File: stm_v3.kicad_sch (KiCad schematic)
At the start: 35 parts, among them Q1 s8050, Q2 s8050, SW1 RST, SW2 BOOT0, U1 STM32L431RCTx, U2 SN65HVD231, Y1 16 MHz

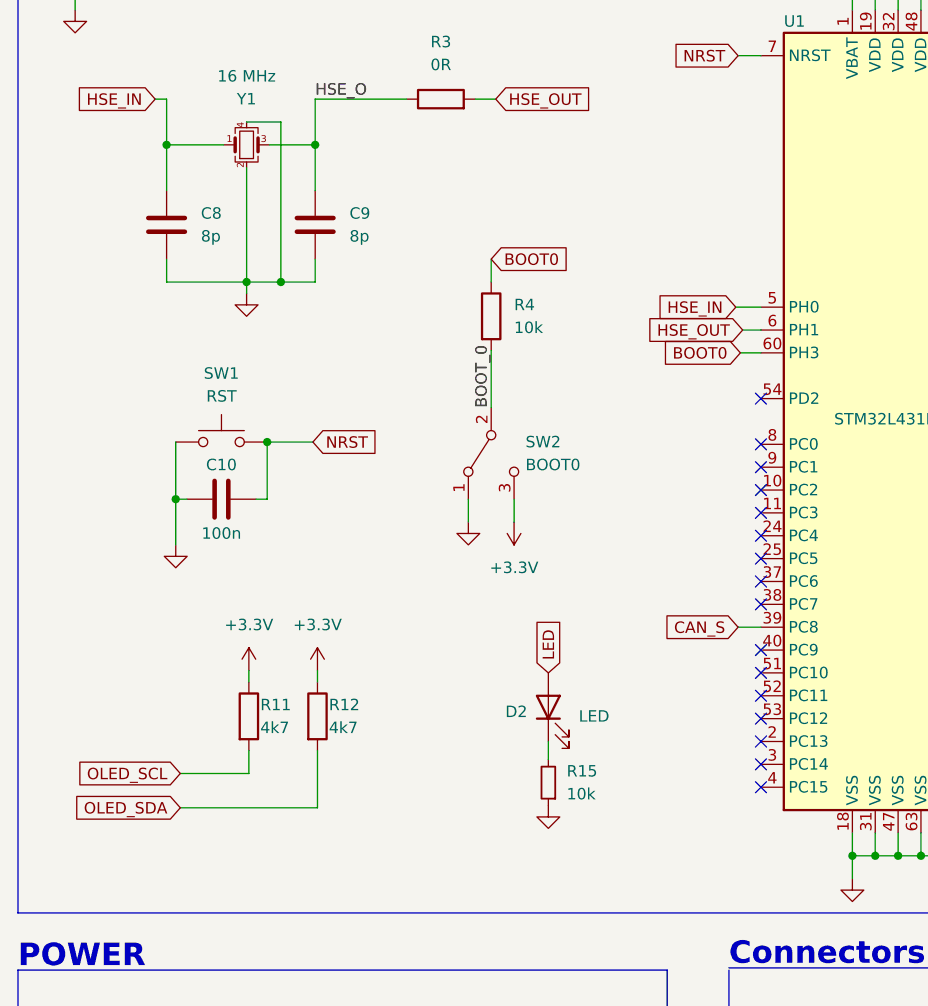
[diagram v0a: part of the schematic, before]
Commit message: Board v2 - reduced size
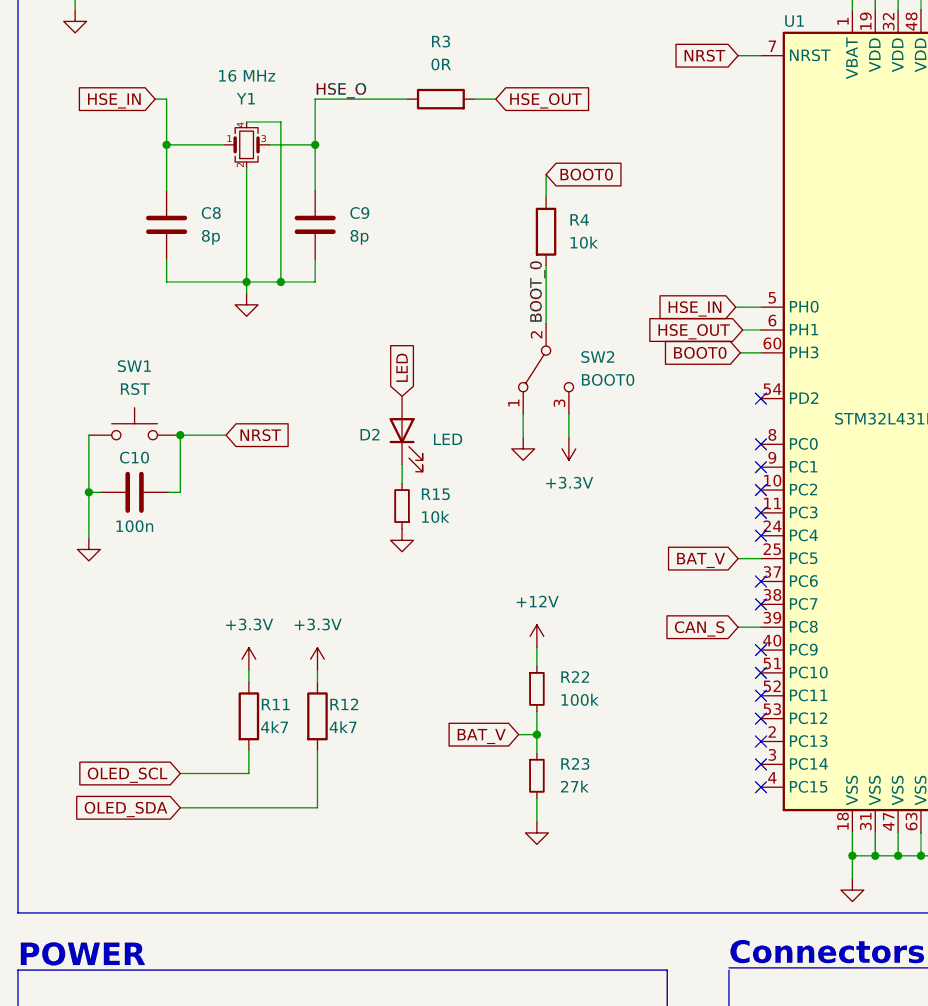
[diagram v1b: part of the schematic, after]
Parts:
- added R22: 100k, Resistor_SMD:R_0402_1005Metric, symbol Device:R_Small
- added R23: 27k, Resistor_SMD:R_0402_1005Metric, symbol Device:R_Small
- C8, C9: footprint Capacitor_SMD:C_0402_1005Metric -> Capacitor_SMD:C_0402_1005Metric_Pad0.74x0.62mm_HandSolder
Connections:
- net +12V: now also R22.1
- net GND: now also R23.2
- net BAT_V: now reaches U1.25 (PC5)
- net BAT_V: now also R22.2, R23.1
- no-connect marks 38 -> 37
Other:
- moved on the sheet: C10, D2, R15, R4, SW1, SW2

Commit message: Further board size reduction
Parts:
- SW1: footprint tme_library:TS-1092S -> tme_library:XKB_TS_1187A
- SW2: footprint tme_library:XKB_SS-3235 -> tme_library:XKB_SS-3292S
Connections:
- net LCD_BTN: now reaches U1.57 (PB5)
- net MENU_BTN: now reaches U1.58 (PB6)
- net BOOT_0 renamed B_0
- no-connect marks 37 -> 35
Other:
- note added: "Connectors & Peripherals"
- note removed: "Connectors"
- moved on the sheet: C10, D2, R11, R12, R15, R22, R23, R3, R4, SW1, SW2

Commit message: KLine update 21/01/23
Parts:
- removed R11, R12: 4k7, Resistor_SMD:R_0402_1005Metric, symbol Device:R
- removed R22: 100k, Resistor_SMD:R_0402_1005Metric, symbol Device:R_Small
- removed R23: 27k, Resistor_SMD:R_0402_1005Metric, symbol Device:R_Small
- R15: value 10k -> 220R
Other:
- moved on the sheet: D2, R15
